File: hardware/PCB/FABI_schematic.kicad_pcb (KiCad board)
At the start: 2 copper layers, 95 x 55 mm, 54 parts, among them J1 PJ307, J2 PJ307, J3 PJ307, J4 PJ307, J5 PJ307, J6 PJ307, J7 PJ307, J8 PJ307, J9 Conn_01x06_Male, SW1 SW_Push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

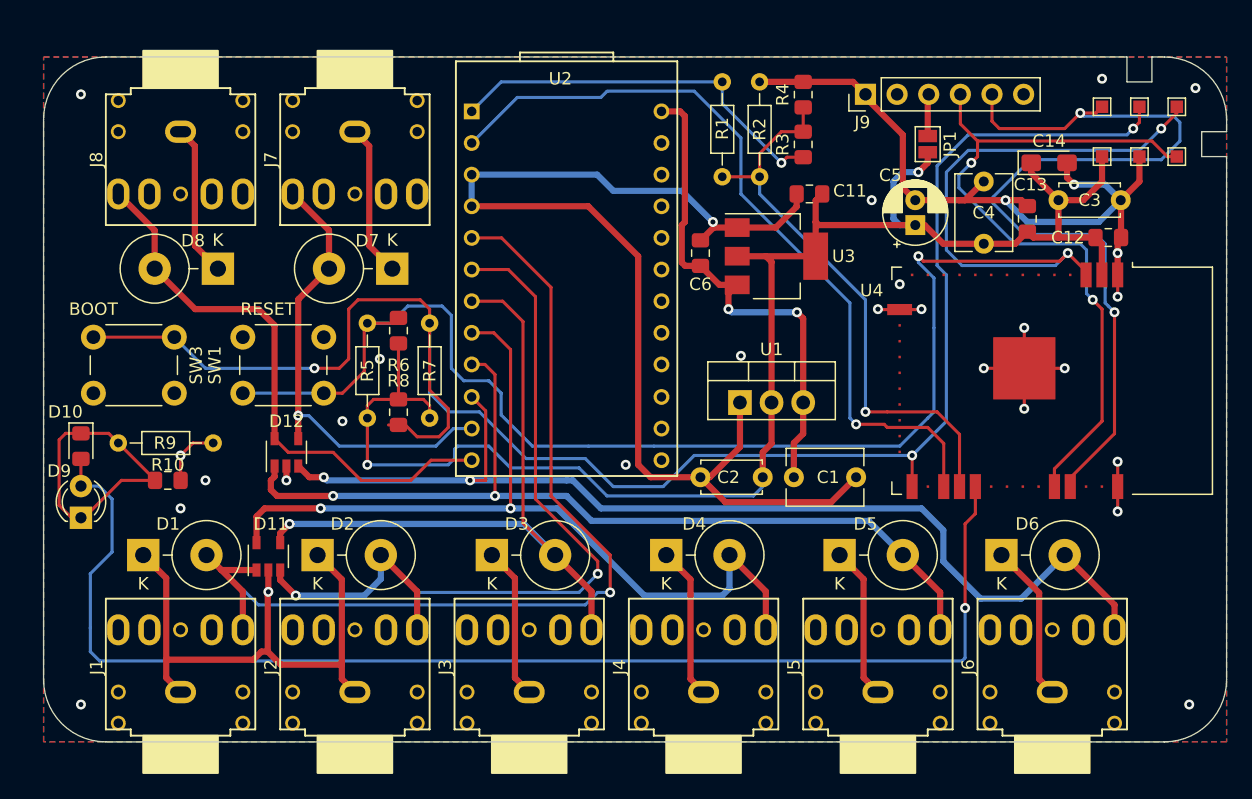
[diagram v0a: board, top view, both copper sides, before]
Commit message: Added logos
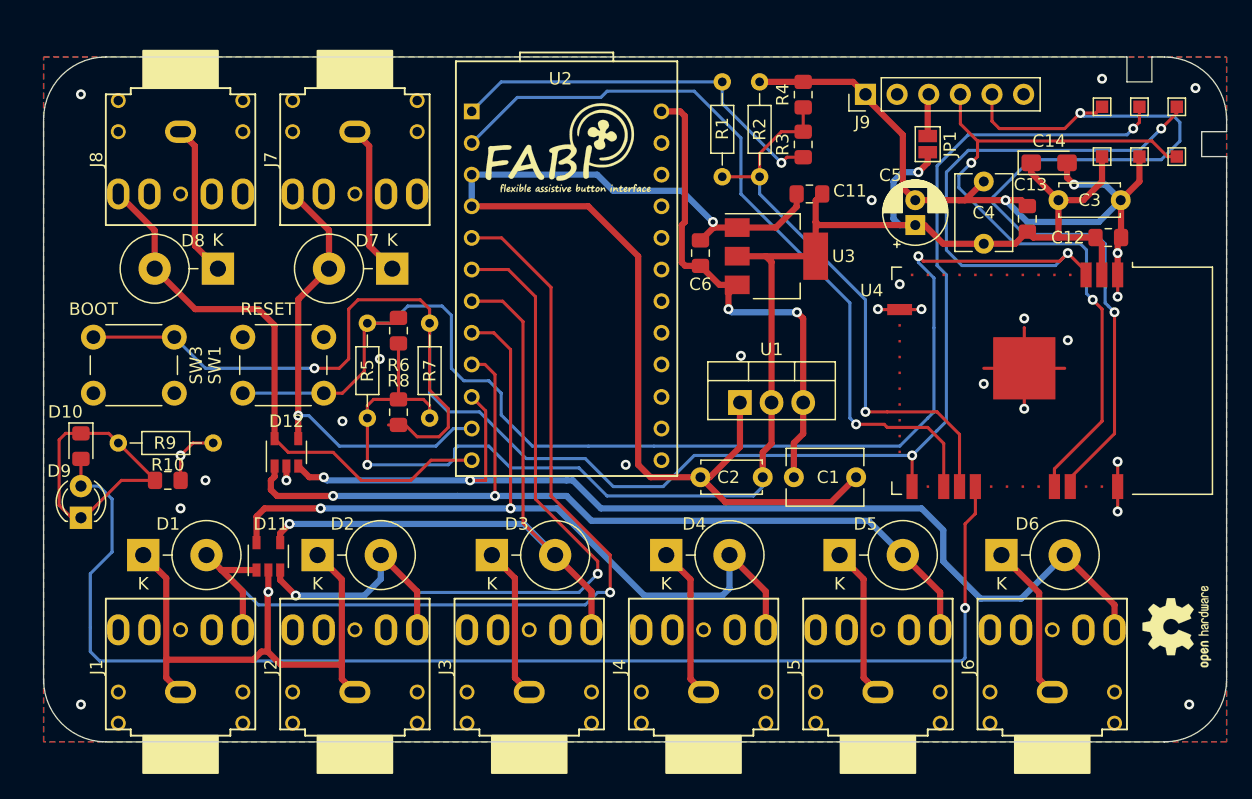
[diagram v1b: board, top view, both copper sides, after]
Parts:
- added G***: LOGO, Logos:MA23LOGO, B.Cu at (93.5, 128.5)
- added G***: LOGO, Logos:FHLOGO, B.Cu at (134.2, 111.5)
- added G***: LOGO, Logos:fabi_15x8, B.Cu at (152.2, 119.2)
- added G***: LOGO, Logos:fabi_15x8, F.Cu at (114.5, 101.2)
- added REF**: KiCad-Logo2_6mm_SilkScreen, Symbol:KiCad-Logo2_6mm_SilkScreen, B.Cu at (154.2, 127.5)
- added REF**: OSHW-Logo2_7.3x6mm_SilkScreen, Symbol:OSHW-Logo2_7.3x6mm_SilkScreen, F.Cu at (164.0, 139.8)
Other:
- board text added: "FABI - Flexible Assistive Button Interface (c) Benjamin Aigner - AsTeRICS Foundation office@asterics-foundation.org"

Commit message: Removed ESP32 from FABI PCB, we will use the FM BT Addon. Added QR codes to UserManual & Releases
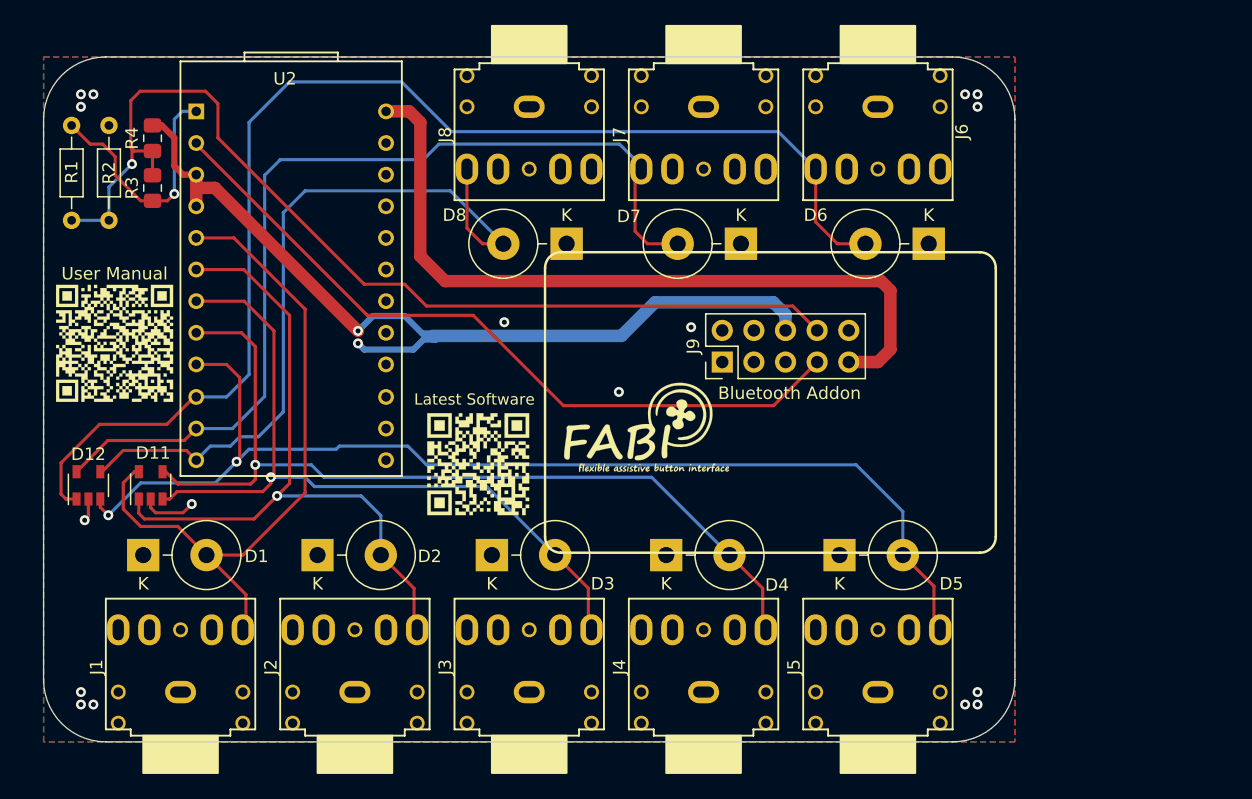
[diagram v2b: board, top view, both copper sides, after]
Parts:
- removed C1, C4: 10u, Capacitor_THT:C_Disc_D6.0mm_W4.4mm_P5.00mm
- removed C11, C12: 100n, Capacitor_SMD:C_0805_2012Metric_Pad1.15x1.40mm_HandSolder
- removed C13, C6: 10u, Capacitor_SMD:C_0805_2012Metric_Pad1.15x1.40mm_HandSolder
- removed C14: 100u, Capacitor_Tantalum_SMD:CP_EIA-3216-12_Kemet-S_Pad1.58x1.35mm_HandSolder
- removed C2, C3: 100n, Capacitor_THT:C_Disc_D4.7mm_W2.5mm_P5.00mm
- removed C5: 100u, Capacitor_THT:CP_Radial_D5.0mm_P2.00mm
- removed D10: LED, LED_SMD:LED_0805_2012Metric_Pad1.15x1.40mm_HandSolder
- removed D9: LED, LED_THT:LED_D3.0mm
- removed the G*** at (152.2, 119.2)
- removed the G*** at (114.5, 101.2)
- removed JP1: SolderJumper_2_Open, Jumper:SolderJumper-2_P1.3mm_Open_Pad1.0x1.5mm
- removed R10: 330R, Resistor_SMD:R_0805_2012Metric_Pad1.15x1.40mm_HandSolder
- removed R5, R7: 10k, Resistor_THT:R_Axial_DIN0204_L3.6mm_D1.6mm_P7.62mm_Horizontal
- removed R6, R8: 10k, Resistor_SMD:R_0805_2012Metric_Pad1.15x1.40mm_HandSolder
- removed R9: 330R, Resistor_THT:R_Axial_DIN0204_L3.6mm_D1.6mm_P7.62mm_Horizontal
- removed REF**: KiCad-Logo2_6mm_SilkScreen, Symbol:KiCad-Logo2_6mm_SilkScreen
- removed REF**: OSHW-Logo2_7.3x6mm_SilkScreen, Symbol:OSHW-Logo2_7.3x6mm_SilkScreen
- removed SW1, SW3: SW_Push, Button_Switch_THT:SW_PUSH_6mm
- removed TP1, TP2, TP3, TP4, TP5, TP6: TestPoint, TestPoint:TestPoint_Pad_1.0x1.0mm
- removed U1: LD1117V33-DG, Package_TO_SOT_THT:TO-220-3_Vertical
- removed U3: NCP1117-3.3, Package_TO_SOT_SMD:SOT-223-3_TabPin2
- removed U4: ESP32-WROOM-32, RF_Module:ESP32-WROOM-32
- added G***: LOGO, QRCodes:QR_releases, F.Cu at (107.9, 126.7)
- added G***: LOGO, QRCodes:QR_pdfmanual, F.Cu at (78.7, 117.0)
- added G***: LOGO, Logos:fabi_15x8, F.Cu at (120.8, 123.7)
- J9: value Conn_01x06_Male -> Conn_02x05_Odd_Even; footprint Connector_PinHeader_2.54mm:PinHeader_1x06_P2.54mm_Vertical -> Connector_PinHeader_2.54mm:PinHeader_2x05_P2.54mm_Vertical
- moved R1 52.4 mm to (75.2, 99.5)
- moved R2 52.4 mm to (78.2, 107.1)
- moved R3 52.4 mm to (81.8, 104.5)
- moved R4 52.4 mm to (81.8, 100.5)
- moved G*** 47.6 mm to (141.1, 127.1)
- moved J6 43.3 mm to (140.0, 101.0), turned to 270 degrees
- moved D7 28.1 mm to (129.0, 109.0)
- moved D8 28.1 mm to (115.0, 109.0)
- moved J7 28.1 mm to (126.0, 101.0)
- moved J8 28.1 mm to (112.0, 101.0)
- moved D6 25.7 mm to (144.1, 109.0), turned to 180 degrees
- moved J9 24.4 mm to (127.5, 118.5)
- moved G*** 22.7 mm to (114.4, 122.6)
- moved U2 22.1 mm to (92.9, 111.0)
- moved D12 16.1 mm to (76.6, 128.4)
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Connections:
- D11 pad 1: 1 -> 2
- D11 pad 3: 2 -> 3
- D11 pad 4: 3 -> 4
- D11 pad 5: 4 -> 1
- D12 pad 1: 5 -> 6
- D12 pad 3: 6 -> 5
- D12 pad 4: 7 -> 8
- D12 pad 5: 8 -> 7
- J9 pad 1: GND -> Net-(J9-Pad1)
- J9 pad 4: /RXD0 -> Net-(J9-Pad4)
- J9 pad 5: /TXD0 -> Net-(J9-Pad5)
- J9 pad 6: Net-(J9-Pad6) -> GND
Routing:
- net GND: track 299.8 -> 78.7 mm, vias 29 -> 19
- net /IO0: track 143.3 -> 0.00 mm, vias 3 -> 0
- net /EN: track 138.2 -> 0.00 mm, vias 3 -> 0
- net +3V3: track 130.2 -> 0.00 mm, vias 2 -> 0
- net /LED: track 102.8 -> 0.00 mm, vias 1 -> 0
- net /TXD0: track 70.8 -> 0.00 mm, vias 2 -> 0
- net /RXD0: track 58.6 -> 0.00 mm, vias 2 -> 0
- net 7: track 37.7 -> 76.7 mm, vias 1 -> 0
- net /ESP_RX: track 45.9 -> 82.1 mm
- net Net-(D10-Pad1): track 24.1 -> 0.00 mm
- net 1: track 79.0 -> 55.2 mm, vias 1 -> 0
- net VCC: track 40.7 -> 61.3 mm, vias 2 -> 0
- net 5: track 74.1 -> 91.4 mm
- net 6: track 84.9 -> 100.9 mm, vias 2 -> 0
- net 8: track 46.0 -> 61.7 mm
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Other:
- board size 95 x 55 mm -> 78 x 55 mm
- board text added: "Bluetooth Addon"
- board text added: "FABI - Flexible Assistive Button Interface Benjamin Aigner AsTeRICS Foundation / UAS Technikum Wien aignerb@technikum-wien.at office@asterics-foundation.org"
- board text added: "Latest Software"
- board text added: "Supported by:"
- board text added: "User Manual"
- board text removed: "BOOT"
- board text removed: "FABI - Flexible Assistive Button Interface (c) Benjamin Aigner - AsTeRICS Foundation office@asterics-foundation.org"
- board text removed: "RESET"

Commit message: Added Neopixel & MPX pressure sensor to PCB.
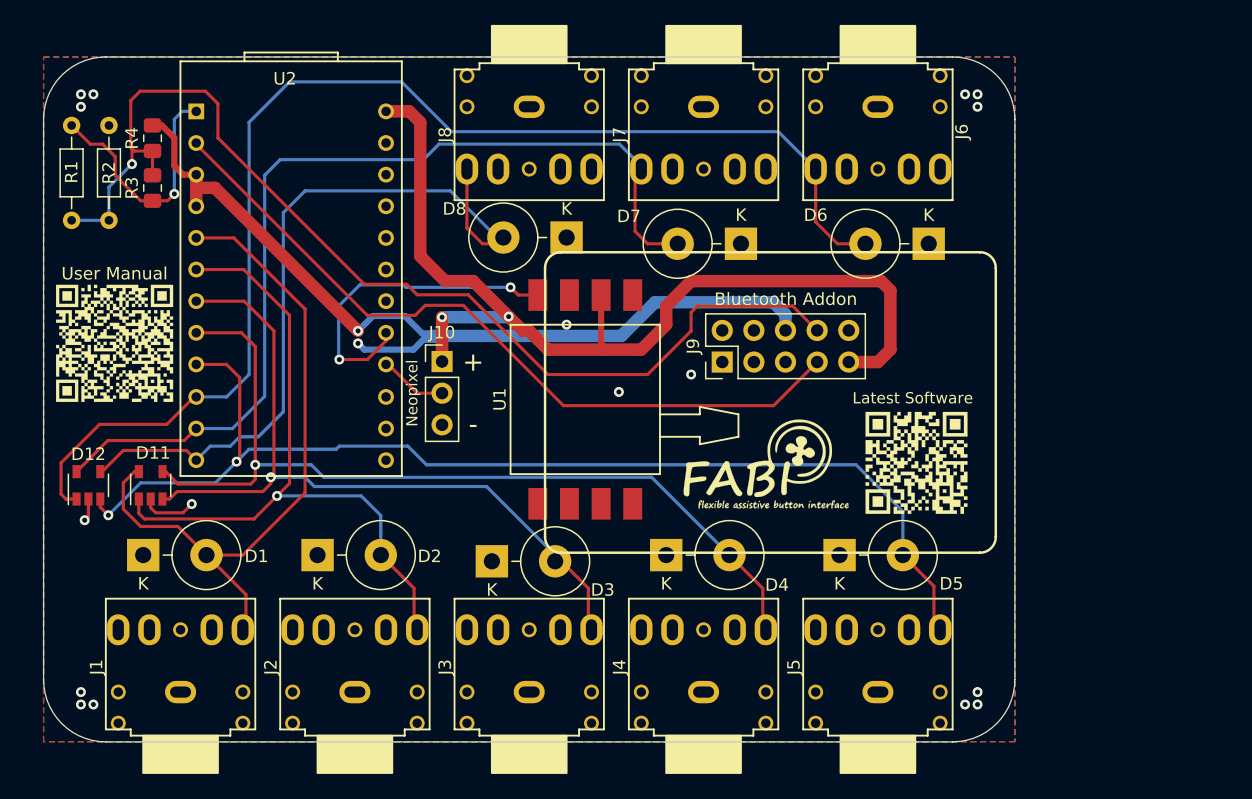
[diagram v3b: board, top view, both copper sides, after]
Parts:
- added G***: LOGO, Logos:fabi_15x8, B.Cu at (77.7, 117.3)
- added J10: Conn_01x03_Male, Connector_PinHeader_2.54mm:PinHeader_1x03_P2.54mm_Vertical, F.Cu at (105.0, 118.5)
- added U1: MPXV7007GP, MPXV7007:MPXV7007GP, F.Cu at (116.5, 121.5)
- moved G*** 35.2 mm to (143.1, 126.6)
- moved G*** 10.0 mm to (130.4, 126.7)
- moved G*** 3.70 mm to (118.1, 122.5)
- moved D3 0.50 mm to (109.0, 134.5)
- moved D8 0.50 mm to (115.0, 108.5)
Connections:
- U2 pad 16: Net-(U2-Pad16) -> /NEOPIXEL
- U2 pad 17: Net-(U2-Pad17) -> /MPX
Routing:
- net /MPX: track 0.00 -> 26.4 mm, vias 0 -> 2
- net VCC: track 61.3 -> 80.1 mm, vias 0 -> 2
- net /ESP_RX: track 82.1 -> 87.6 mm
- net /NEOPIXEL: track 0.00 -> 5.46 mm
- net /A_RX: track 60.1 -> 60.8 mm
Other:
- board text added: "+"
- board text added: "-"
- board text added: "Neopixel"

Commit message: redesign of PCB, Jackplugs updatet, Buzzer added, TVS repositioned
Signed-off-by: fussthalerandreas <fussthaler.andreas1997@gmail.com>
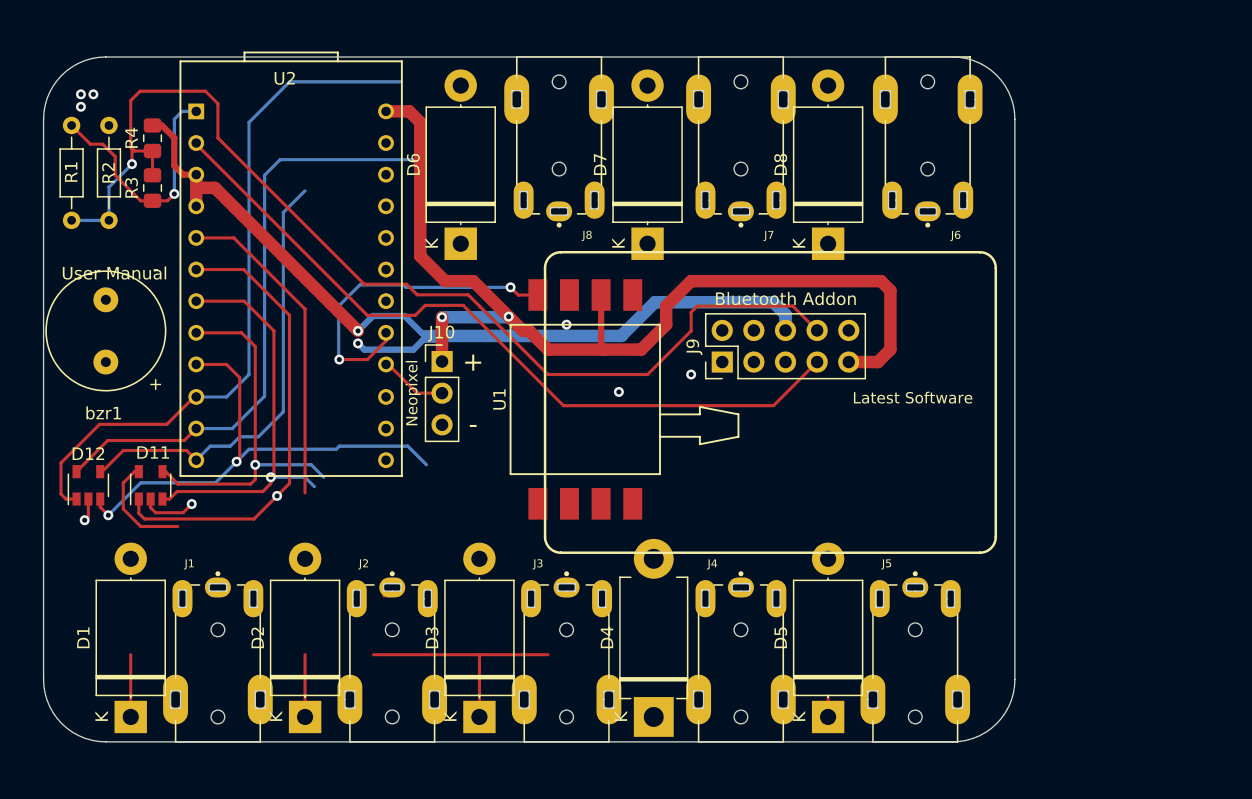
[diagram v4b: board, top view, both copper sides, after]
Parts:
- removed G*** (x2): LOGO, Logos:fabi_15x8
- removed G***: LOGO, QRCodes:QR_releases
- removed G***: LOGO, QRCodes:QR_pdfmanual
- removed G***: LOGO, Logos:FHLOGO
- removed G***: LOGO, Logos:MA23LOGO
- added bzr1: CMI-9605IC-0380T, CMI-9605IC-0380T:CUI_CMI-9605IC-0380T, F.Cu at (78.0, 116.0)
- D1, D2, D3, D5, D6, D7, D8: footprint Diode_THT:D_DO-201AE_P5.08mm_Vertical_KathodeUp -> Diode_THT:D_DO-201AE_P12.70mm_Horizontal
- D4: footprint Diode_THT:D_DO-201AE_P5.08mm_Vertical_KathodeUp -> Diode_THT:D_DO-201AD_P12.70mm_Horizontal
- J1, J2, J3, J4, J5, J6, J7, J8: value PJ307 -> Cliff_68125; footprint PJ307:PJ-307 -> CLIFF_FC68125:CLIFF_FC68125
- moved D6 37.6 mm to (106.5, 109.0), turned to 90 degrees
- moved D8 21.0 mm to (136.0, 109.0), turned to 90 degrees
- moved D1 13.0 mm to (80.0, 147.0), turned to 90 degrees
- moved D2 13.0 mm to (94.0, 147.0), turned to 90 degrees
- moved D4 13.0 mm to (122.0, 147.0), turned to 90 degrees
- moved D5 13.0 mm to (136.0, 147.0), turned to 90 degrees
- moved D3 12.5 mm to (108.0, 147.0), turned to 90 degrees
- moved D7 7.50 mm to (121.5, 109.0), turned to 90 degrees
- moved J6 4.47 mm to (144.0, 103.0), turned to 180 degrees
- moved J1 3.61 mm to (87.0, 140.0), turned to 0 degrees
- moved J2 3.61 mm to (101.0, 140.0), turned to 0 degrees
- moved J3 3.61 mm to (115.0, 140.0), turned to 0 degrees
- moved J4 3.61 mm to (129.0, 140.0), turned to 0 degrees
- moved J5 3.61 mm to (143.0, 140.0), turned to 0 degrees
- moved J7 3.61 mm to (129.0, 103.0), turned to 180 degrees
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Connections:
- J9 pad 1: Net-(J9-Pad1) -> (no net)
- J9 pad 2: Net-(J9-Pad2) -> (no net)
- J9 pad 3: Net-(J9-Pad3) -> (no net)
- J9 pad 4: Net-(J9-Pad4) -> (no net)
- J9 pad 5: Net-(J9-Pad5) -> (no net)
- U1 pad 1: Net-(U1-Pad1) -> (no net)
- U1 pad 5: Net-(U1-Pad5) -> (no net)
- U1 pad 6: Net-(U1-Pad6) -> (no net)
- U1 pad 7: Net-(U1-Pad7) -> (no net)
- U1 pad 8: Net-(U1-Pad8) -> (no net)
- U2 pad 13: Net-(U2-Pad13) -> (no net)
- U2 pad 14: Net-(U2-Pad14) -> (no net)
- U2 pad 15: Net-(U2-Pad15) -> (no net)
- U2 pad 18: Net-(U2-Pad18) -> buzzer_pin
- U2 pad 19: Net-(U2-Pad19) -> (no net)
- U2 pad 20: Net-(U2-Pad20) -> (no net)
- U2 pad 21: Net-(U2-Pad21) -> (no net)
- U2 pad 22: Net-(U2-Pad22) -> (no net)
- U2 pad 23: Net-(U2-Pad23) -> (no net)
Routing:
- net 5: track 91.4 -> 40.8 mm
- net 6: track 100.9 -> 55.8 mm
- net 4: track 72.2 -> 29.8 mm
- net GND: track 78.7 -> 109.2 mm, vias 19 -> 10
- net 3: track 61.4 -> 32.6 mm
- net 7: track 76.7 -> 48.6 mm
- net 8: track 61.7 -> 35.8 mm
- net 1: track 55.2 -> 34.5 mm
- net 2: track 56.5 -> 37.1 mm
- net (no net): track 0.00 -> 0.52 mm
- removed copper zone on B.Cu, net GND
- removed copper zone on F.Cu, net GND
